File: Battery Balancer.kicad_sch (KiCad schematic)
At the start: 22 parts, among them Q6 Vishay sir404dp, or SiR500DP, U1 BQ76905RGRR

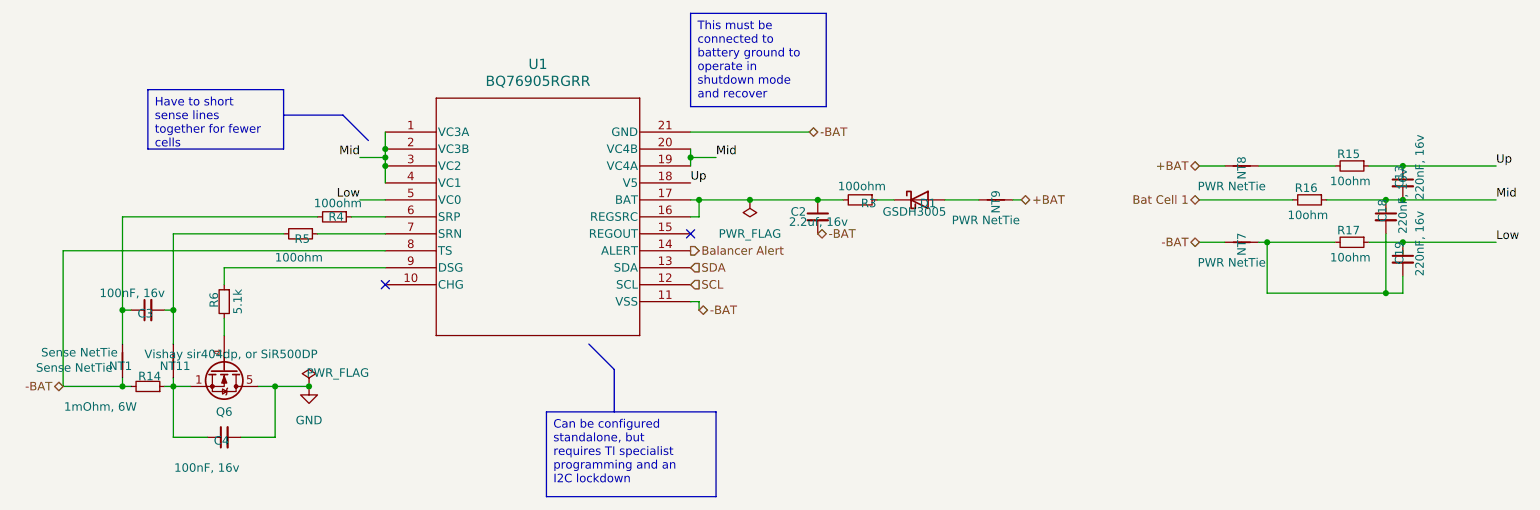
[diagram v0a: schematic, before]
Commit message: Updated to kicad 9
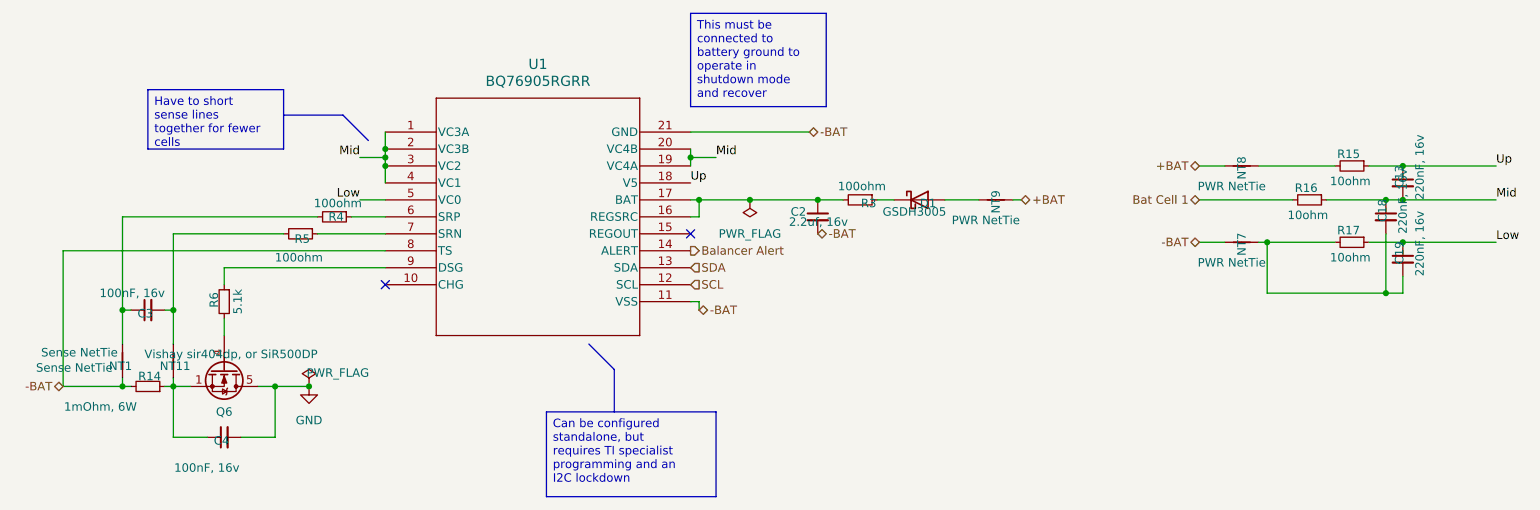
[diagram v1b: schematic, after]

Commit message: Revert update of pmosfets with large pad 5
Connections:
- net GND: no longer Q6.6 (D), Q6.7 (D), Q6.8 (D)
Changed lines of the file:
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@@
 		(pin "5"
-		)
-		(pin "7"
-		)
-		(pin "8"
-		)
-		(pin "6"
 		)
 		(instances
